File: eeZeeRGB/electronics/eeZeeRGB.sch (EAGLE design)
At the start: 5 parts

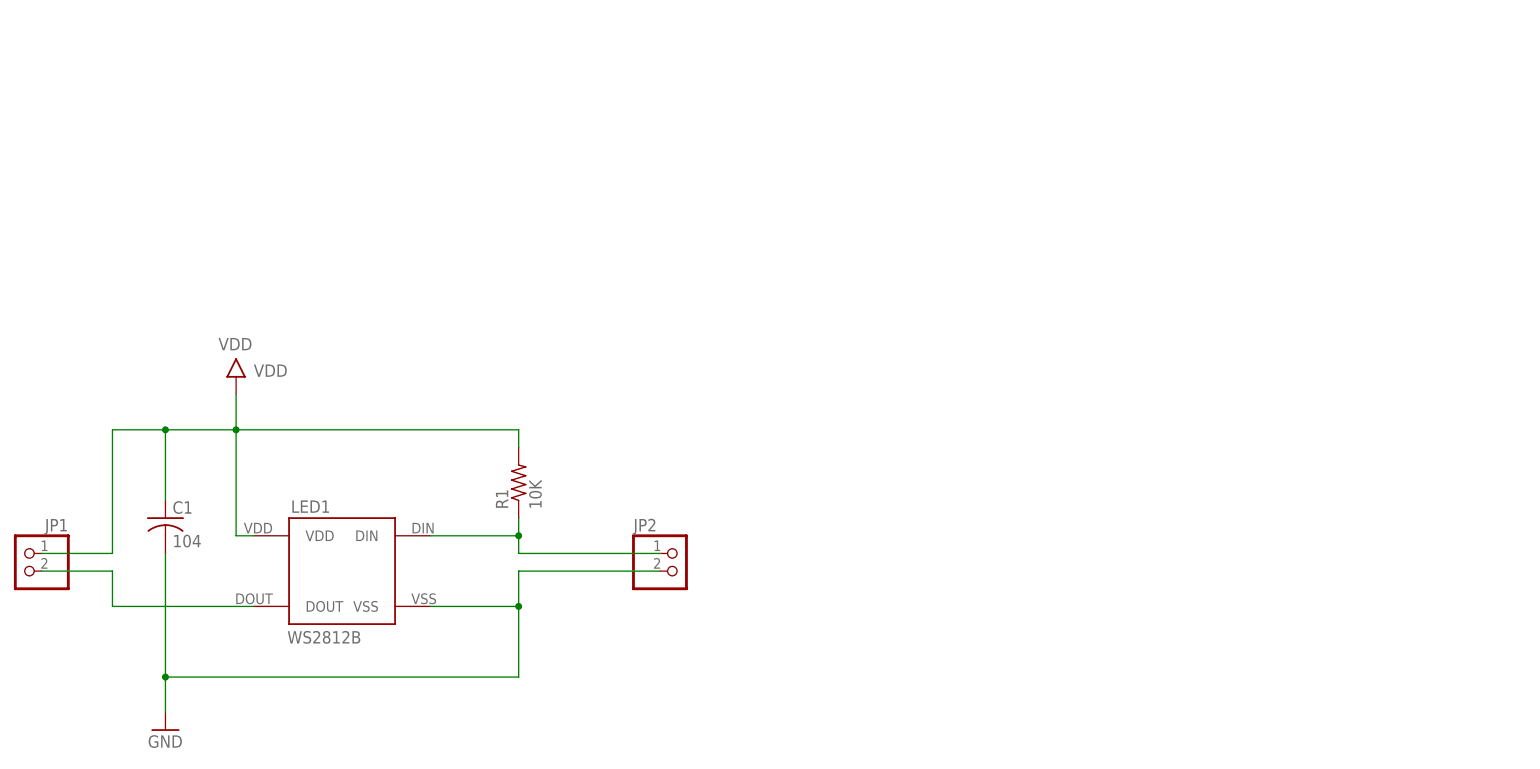
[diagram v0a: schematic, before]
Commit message: Added project documentation box thingy.
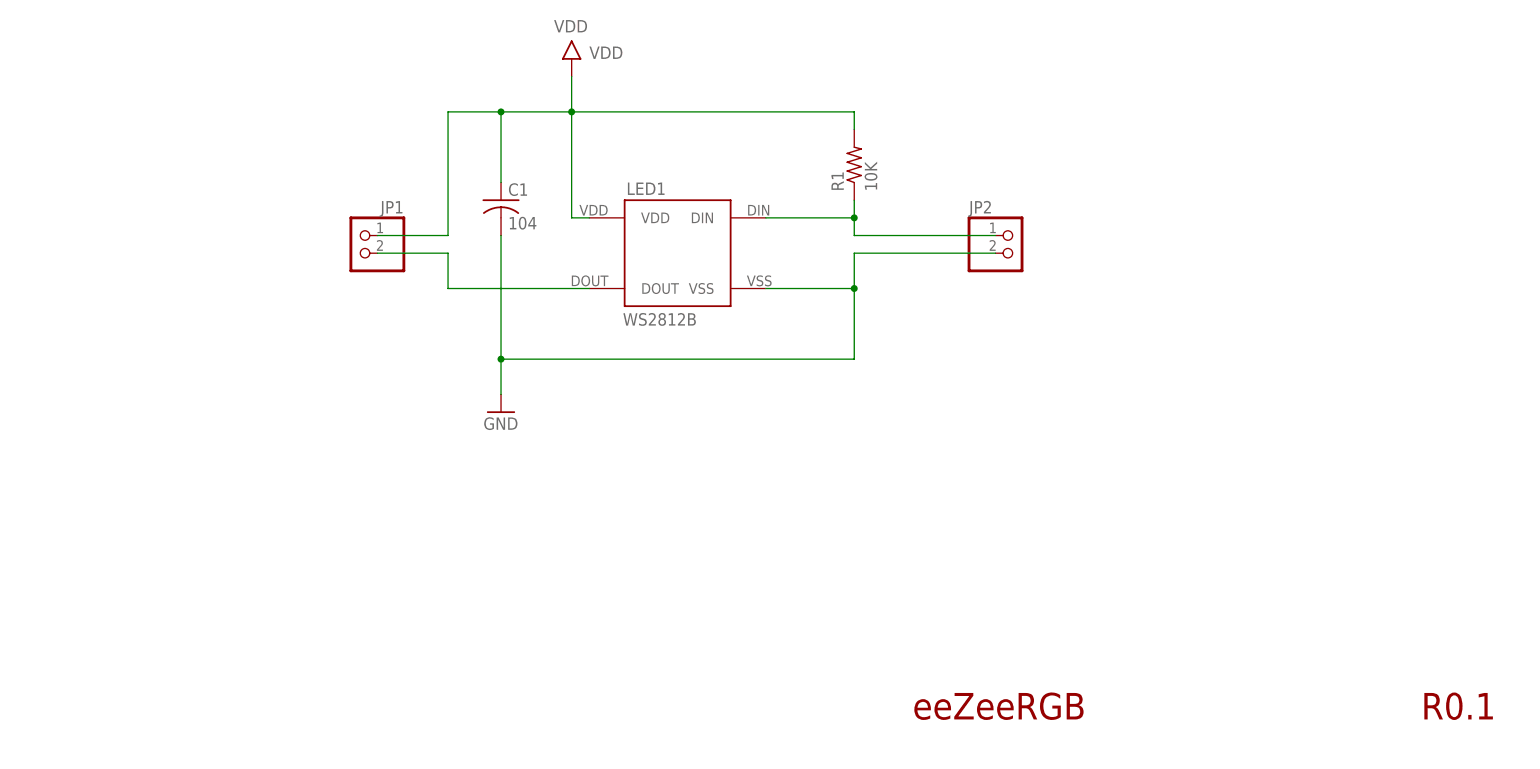
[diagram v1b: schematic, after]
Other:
- note added: "R0.1"
- note added: "eeZeeRGB"
- moved on the sheet: C1, JP1, JP2, LED1, R1
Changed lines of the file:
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@@
 <part name="U$1" library="bt" deviceset="VDD" device=""/>
 <part name="GND1" library="bt" deviceset="GND" device=""/>
+<part name="FRAME1" library="bt" deviceset="LETTER_L" device=""/>
 </parts>
 <sheets>
 <sheet>
 <plain>
+<text x="158.242" y="24.384" size="3.81" layer="94">eeZeeRGB</text>
+<text x="231.394" y="24.384" size="3.81" layer="94">R0.1</text>
 </plain>
 <instances>
-<instance part="R1" gate="G$1" x="101.6" y="58.42" rot="R90"/>
-<instance part="C1" gate="G$1" x="50.8" y="53.34"/>
-<instance part="LED1" gate="G$1" x="76.2" y="45.72"/>
-<instance part="JP1" gate="A" x="30.48" y="45.72" rot="MR0"/>
-<instance part="JP2" gate="A" x="124.46" y="45.72"/>
-<instance part="U$1" gate="G$1" x="60.96" y="73.66"/>
-<instance part="GND1" gate="1" x="50.8" y="22.86"/>
+<instance part="R1" gate="G$1" x="149.86" y="104.14" rot="R90"/>
+<instance part="C1" gate="G$1" x="99.06" y="99.06"/>
+<instance part="LED1" gate="G$1" x="124.46" y="91.44"/>
+<instance part="JP1" gate="A" x="78.74" y="91.44" rot="MR0"/>
+<instance part="JP2" gate="A" x="172.72" y="91.44"/>
+<instance part="U$1" gate="G$1" x="109.22" y="119.38"/>
+<instance part="GND1" gate="1" x="99.06" y="68.58"/>
+<instance part="FRAME1" gate="G$1" x="0" y="0"/>
+<instance part="FRAME1" gate="G$2" x="147.32" y="2.54"/>
 </instances>
 <busses>
@@
 <segment>
 <pinref part="LED1" gate="G$1" pin="DOUT"/>
-<wire x1="63.5" y1="40.64" x2="43.18" y2="40.64" width="0.1524" layer="91"/>
-<wire x1="43.18" y1="40.64" x2="43.18" y2="45.72" width="0.1524" layer="91"/>
+<wire x1="111.76" y1="86.36" x2="91.44" y2="86.36" width="0.1524" layer="91"/>
+<wire x1="91.44" y1="86.36" x2="91.44" y2="91.44" width="0.1524" layer="91"/>
 <pinref part="JP1" gate="A" pin="2"/>
-<wire x1="43.18" y1="45.72" x2="33.02" y2="45.72" width="0.1524" layer="91"/>
+<wire x1="91.44" y1="91.44" x2="81.28" y2="91.44" width="0.1524" layer="91"/>
 </segment>
 </net>
@@
 <segment>
 <pinref part="JP2" gate="A" pin="1"/>
-<wire x1="121.92" y1="48.26" x2="101.6" y2="48.26" width="0.1524" layer="91"/>
-<wire x1="101.6" y1="48.26" x2="101.6" y2="50.8" width="0.1524" layer="91"/>
+<wire x1="170.18" y1="93.98" x2="149.86" y2="93.98" width="0.1524" layer="91"/>
+<wire x1="149.86" y1="93.98" x2="149.86" y2="96.52" width="0.1524" layer="91"/>
 <pinref part="LED1" gate="G$1" pin="DIN"/>
 <pinref part="R1" gate="G$1" pin="1"/>
-<wire x1="88.9" y1="50.8" x2="101.6" y2="50.8" width="0.1524" layer="91"/>
-<wire x1="101.6" y1="50.8" x2="101.6" y2="53.34" width="0.1524" layer="91"/>
-<junction x="101.6" y="50.8"/>
+<wire x1="137.16" y1="96.52" x2="149.86" y2="96.52" width="0.1524" layer="91"/>
+<wire x1="149.86" y1="96.52" x2="149.86" y2="99.06" width="0.1524" layer="91"/>
+<junction x="149.86" y="96.52"/>
 </segment>
 </net>
@@
 <segment>
 <pinref part="C1" gate="G$1" pin="2"/>
-<wire x1="50.8" y1="48.26" x2="50.8" y2="30.48" width="0.1524" layer="91"/>
+<wire x1="99.06" y1="93.98" x2="99.06" y2="76.2" width="0.1524" layer="91"/>
 <pinref part="LED1" gate="G$1" pin="VSS"/>
-<wire x1="101.6" y1="40.64" x2="88.9" y2="40.64" width="0.1524" layer="91"/>
-<wire x1="50.8" y1="30.48" x2="101.6" y2="30.48" width="0.1524" layer="91"/>
-<wire x1="101.6" y1="30.48" x2="101.6" y2="40.64" width="0.1524" layer="91"/>
+<wire x1="149.86" y1="86.36" x2="137.16" y2="86.36" width="0.1524" layer="91"/>
+<wire x1="99.06" y1="76.2" x2="149.86" y2="76.2" width="0.1524" layer="91"/>
+<wire x1="149.86" y1="76.2" x2="149.86" y2="86.36" width="0.1524" layer="91"/>
 <pinref part="JP2" gate="A" pin="2"/>
-<wire x1="121.92" y1="45.72" x2="101.6" y2="45.72" width="0.1524" layer="91"/>
-<wire x1="101.6" y1="45.72" x2="101.6" y2="40.64" width="0.1524" layer="91"/>
-<junction x="101.6" y="40.64"/>
+<wire x1="170.18" y1="91.44" x2="149.86" y2="91.44" width="0.1524" layer="91"/>
+<wire x1="149.86" y1="91.44" x2="149.86" y2="86.36" width="0.1524" layer="91"/>
+<junction x="149.86" y="86.36"/>
 <pinref part="GND1" gate="1" pin="GND"/>
-<wire x1="50.8" y1="25.4" x2="50.8" y2="30.48" width="0.1524" layer="91"/>
-<junction x="50.8" y="30.48"/>
+<wire x1="99.06" y1="71.12" x2="99.06" y2="76.2" width="0.1524" layer="91"/>
+<junction x="99.06" y="76.2"/>
 </segment>
 </net>
@@
 <segment>
 <pinref part="R1" gate="G$1" pin="2"/>
-<wire x1="50.8" y1="66.04" x2="60.96" y2="66.04" width="0.1524" layer="91"/>
-<wire x1="60.96" y1="66.04" x2="101.6" y2="66.04" width="0.1524" layer="91"/>
-<wire x1="101.6" y1="66.04" x2="101.6" y2="63.5" width="0.1524" layer="91"/>
+<wire x1="99.06" y1="111.76" x2="109.22" y2="111.76" width="0.1524" layer="91"/>
+<wire x1="109.22" y1="111.76" x2="149.86" y2="111.76" width="0.1524" layer="91"/>
+<wire x1="149.86" y1="111.76" x2="149.86" y2="109.22" width="0.1524" layer="91"/>
 <pinref part="C1" gate="G$1" pin="1"/>
-<wire x1="50.8" y1="55.88" x2="50.8" y2="66.04" width="0.1524" layer="91"/>
+<wire x1="99.06" y1="101.6" x2="99.06" y2="111.76" width="0.1524" layer="91"/>
 <pinref part="LED1" gate="G$1" pin="VDD"/>
-<wire x1="63.5" y1="50.8" x2="60.96" y2="50.8" width="0.1524" layer="91"/>
-<wire x1="60.96" y1="50.8" x2="60.96" y2="66.04" width="0.1524" layer="91"/>
+<wire x1="111.76" y1="96.52" x2="109.22" y2="96.52" width="0.1524" layer="91"/>
+<wire x1="109.22" y1="96.52" x2="109.22" y2="111.76" width="0.1524" layer="91"/>
 <pinref part="JP1" gate="A" pin="1"/>
-<wire x1="33.02" y1="48.26" x2="43.18" y2="48.26" width="0.1524" layer="91"/>
-<wire x1="43.18" y1="48.26" x2="43.18" y2="66.04" width="0.1524" layer="91"/>
-<wire x1="43.18" y1="66.04" x2="50.8" y2="66.04" width="0.1524" layer="91"/>
-<junction x="50.8" y="66.04"/>
-<junction x="60.96" y="66.04"/>
+<wire x1="81.28" y1="93.98" x2="91.44" y2="93.98" width="0.1524" layer="91"/>
+<wire x1="91.44" y1="93.98" x2="91.44" y2="111.76" width="0.1524" layer="91"/>
+<wire x1="91.44" y1="111.76" x2="99.06" y2="111.76" width="0.1524" layer="91"/>
+<junction x="99.06" y="111.76"/>
+<junction x="109.22" y="111.76"/>
 <pinref part="U$1" gate="G$1" pin="VDD"/>
-<wire x1="60.96" y1="66.04" x2="60.96" y2="71.12" width="0.1524" layer="91"/>
+<wire x1="109.22" y1="111.76" x2="109.22" y2="116.84" width="0.1524" layer="91"/>
 </segment>
 </net>
